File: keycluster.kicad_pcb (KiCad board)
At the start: 2 copper layers, 45.1 x 52.6 mm, 62 parts, among them P2 CONN_5, P7 CONN_10, P8 CONN_7, U1 MKL03Z32VFK4, U2 IS31FL3737, U4 ESD

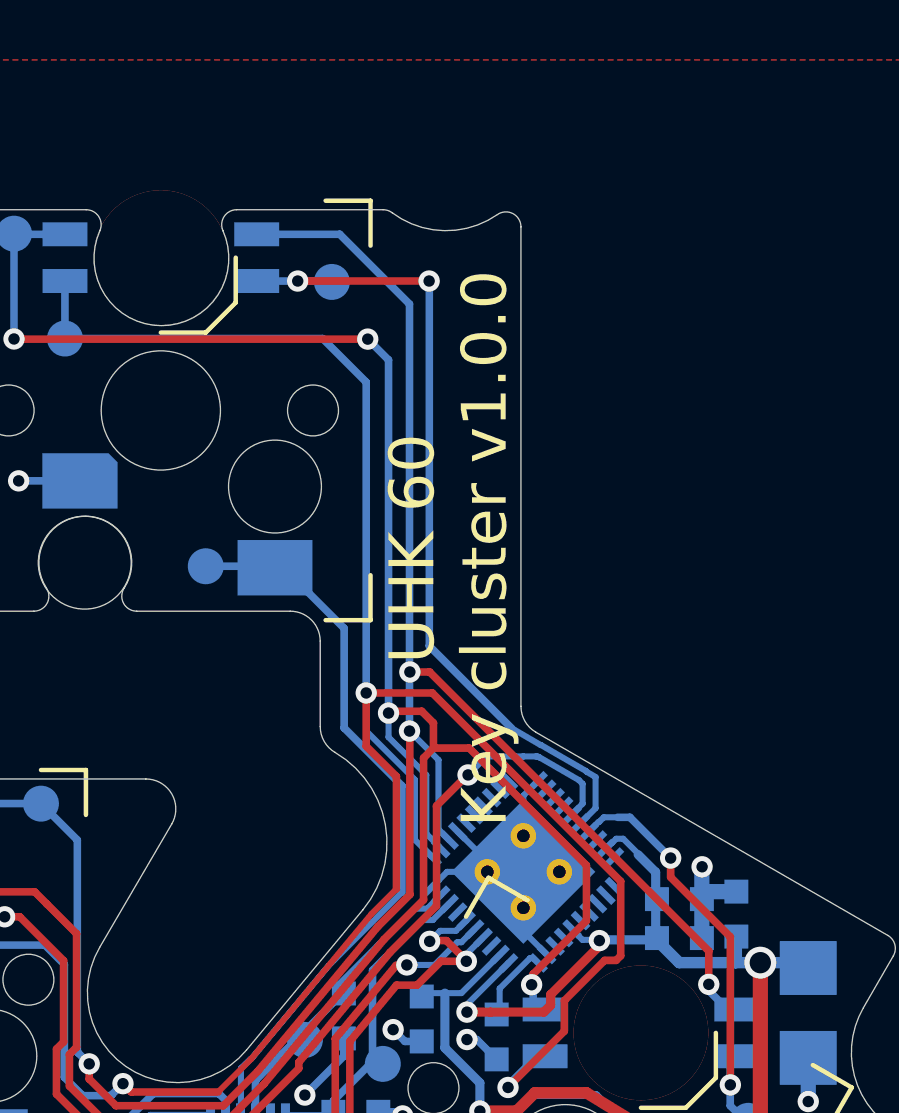
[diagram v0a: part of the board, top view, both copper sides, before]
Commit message: Improve silk screen.
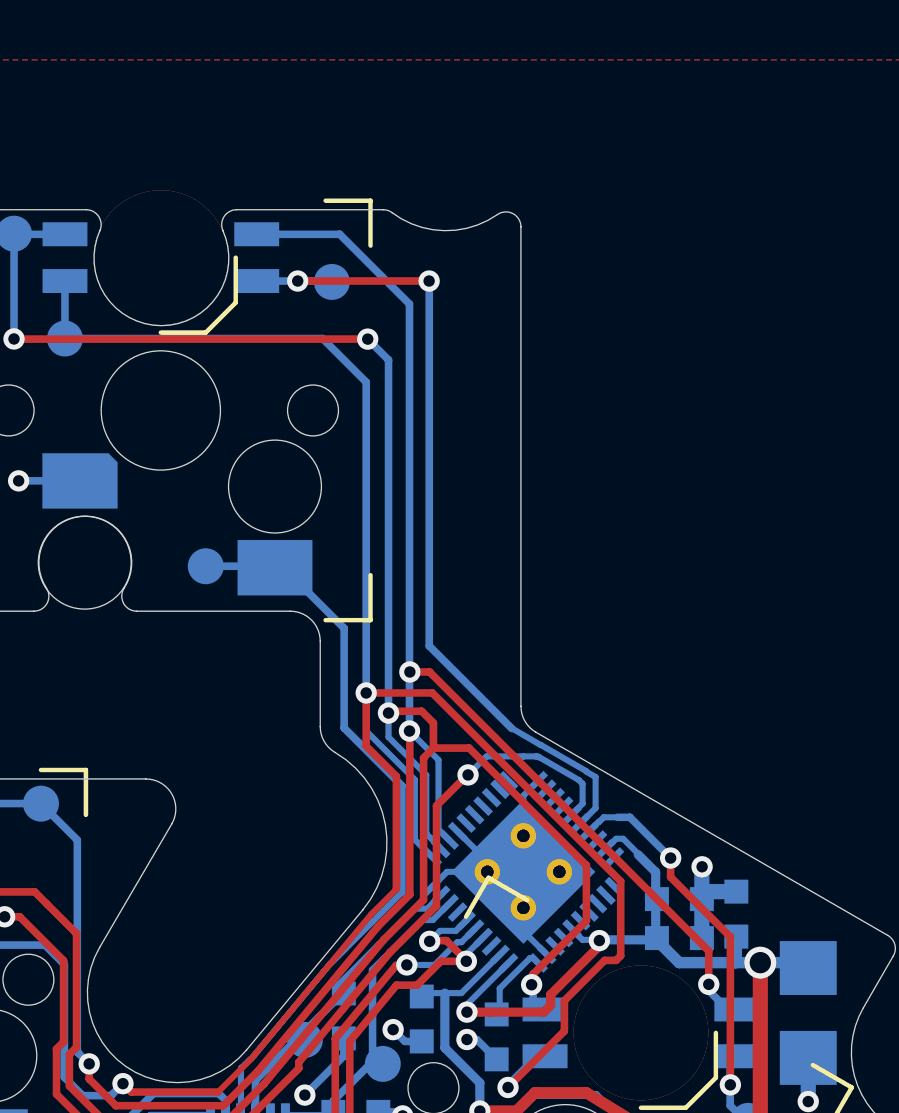
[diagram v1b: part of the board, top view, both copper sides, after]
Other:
- board text added: "PCB ID: keycluster_main_1.0.0"
- board text removed: "UHK 60 Key cluster v1.0.0"
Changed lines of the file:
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@@
     (pcb_text_size 1.5 1.5)
     (mod_edge_width 0.15)
-    (mod_text_size 1 1)
+    (mod_text_size 0.75 0.75)
     (mod_text_width 0.15)
     (pad_size 1.5 1.5)
@@
       (effects (font (size 0.75 0.75) (thickness 0.15)) (justify mirror))
     )
-    (fp_text value GND (at 0 1.3) (layer B.SilkS)
+    (fp_text value GND (at -1.4 1.3) (layer B.SilkS)
       (effects (font (size 0.75 0.75) (thickness 0.15)) (justify mirror))
     )
@@
     )
   )
-  (gr_text "UHK 60\nKey cluster v1.0.0" (at 152.309512 92.310302 90) (layer F.SilkS)
-    (effects (font (size 1.5 1.5) (thickness 0.3)))
+  (gr_text "PCB ID: keycluster_main_1.0.0" (at 164.809512 121.810302 240) (layer B.SilkS)
+    (effects (font (size 0.75 0.75) (thickness 0.15)) (justify mirror))
   )
   (gr_line (start 129.009512 114.110302) (end 132.809512 113.310302) (layer B.SilkS) (width 0.2))

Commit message: Show silk screen values.
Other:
- board text added: "U1 P/N:"

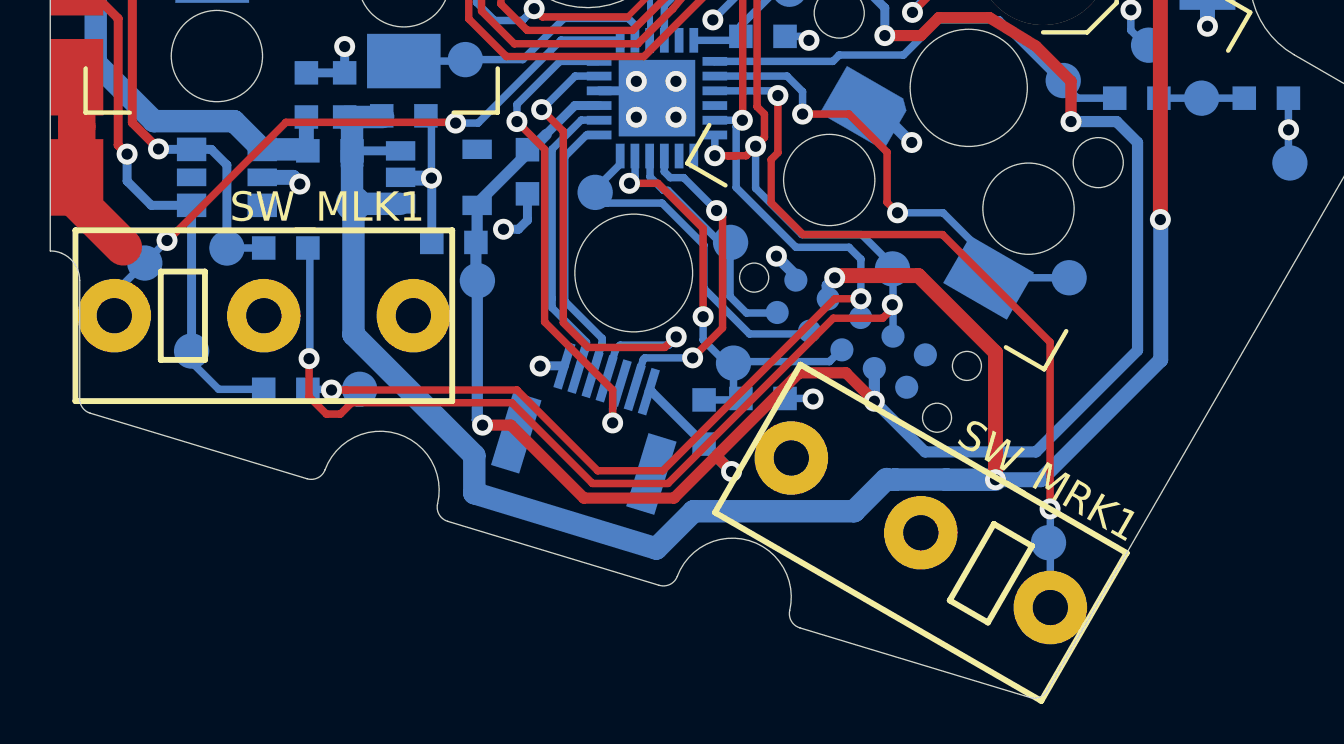
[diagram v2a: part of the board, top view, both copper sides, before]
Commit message: Update buttons.
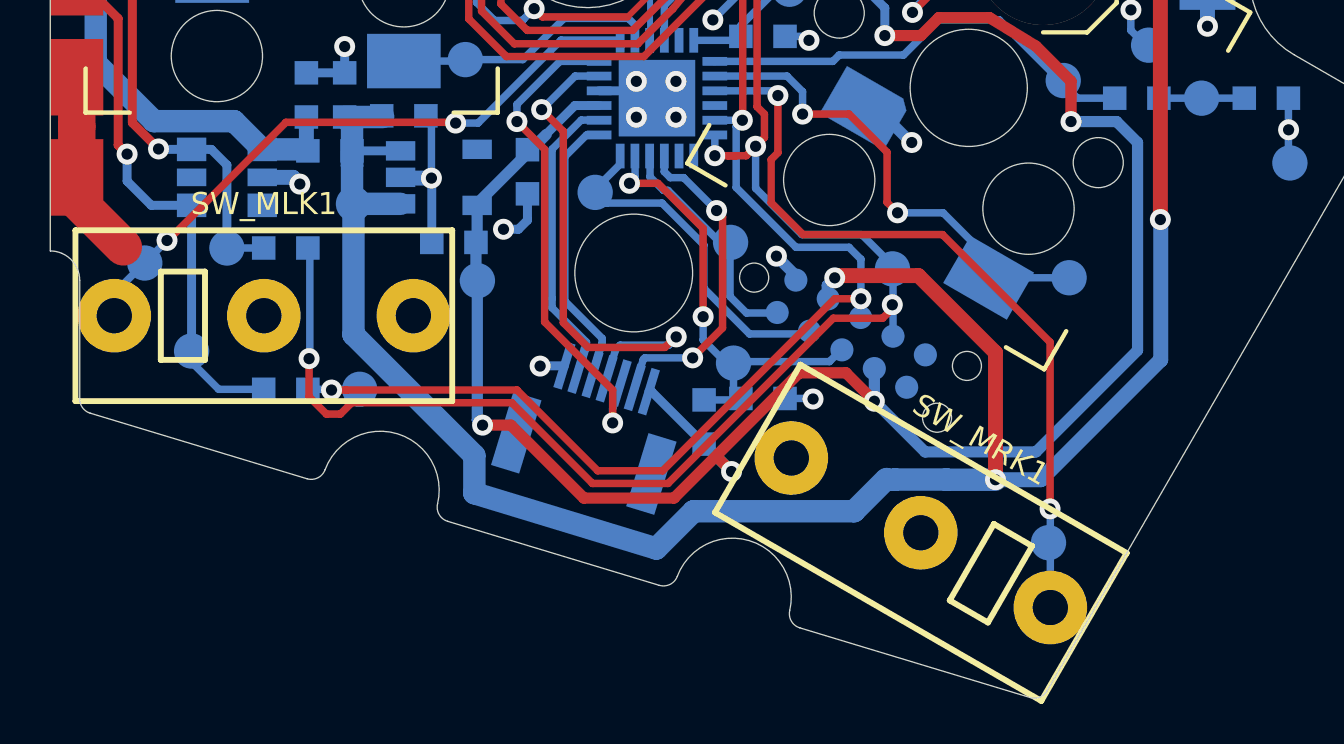
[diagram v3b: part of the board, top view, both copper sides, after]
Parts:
- SW_MLK1, SW_MRK1: footprint ugl:CMI126603D08 -> UGL:CMI126603D08
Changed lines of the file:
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@@
     (add_net "Net-(VR1-Pad4)")
+  )
+  (module UGL:CMI126603D08 locked (layer F.Cu)
+    (at 154.572235 127.973381 150)
+    (fp_text reference SW_MRK1 (at -0.182794 3.757945 150) (layer F.SilkS)
+      (effects (font (size 0.75 0.75) (thickness 0.15)))
+    )
+    (fp_text value MRK (at 0 3.9 150) (layer F.Fab) hide
+      (effects (font (size 0.75 0.75) (thickness 0.15)))
+    )
+    (fp_line (start -3.5 1.5) (end -3.5 -1.5) (layer F.SilkS) (width 0.2))
+    (fp_line (start -2 1.5) (end -3.5 1.5) (layer F.SilkS) (width 0.2))
+    (fp_line (start -2 -1.5) (end -2 1.5) (layer F.SilkS) (width 0.2))
+    (fp_line (start -3.5 -1.5) (end -2 -1.5) (layer F.SilkS) (width 0.2))
+    (fp_line (start 6.4 -2.9) (end 6.4 2.9) (layer F.SilkS) (width 0.2))
+    (fp_line (start -6.4 2.9) (end 6.4 2.9) (layer F.SilkS) (width 0.2))
+    (fp_line (start -6.4 -2.9) (end -6.4 2.9) (layer F.SilkS) (width 0.2))
+    (fp_line (start 6.4 -2.9) (end -6.4 -2.9) (layer F.SilkS) (width 0.2))
+    (pad 3 thru_hole circle (at 5.08 0 150) (size 2.5 2.5) (drill 1.2) (layers *.Cu *.Mask))
+    (pad 2 thru_hole circle (at 0 0 150) (size 2.5 2.5) (drill 1.2) (layers *.Cu *.Mask)
+      (net 1 GND))
+    (pad 1 thru_hole circle (at -5.08 0 150) (size 2.5 2.5) (drill 1.2) (layers *.Cu *.Mask)
+      (net 6 /KEY_MRIGHT))
+  )
+  (module UGL:CMI126603D08 locked (layer F.Cu)
+    (at 132.254409 120.600007)
+    (fp_text reference SW_MLK1 (at 0 -3.8) (layer F.SilkS)
+      (effects (font (size 0.75 0.75) (thickness 0.15)))
+    )
+    (fp_text value MLK (at 0 3.9) (layer F.Fab) hide
+      (effects (font (size 0.75 0.75) (thickness 0.15)))
+    )
+    (fp_line (start -3.5 1.5) (end -3.5 -1.5) (layer F.SilkS) (width 0.2))
+    (fp_line (start -2 1.5) (end -3.5 1.5) (layer F.SilkS) (width 0.2))
+    (fp_line (start -2 -1.5) (end -2 1.5) (layer F.SilkS) (width 0.2))
+    (fp_line (start -3.5 -1.5) (end -2 -1.5) (layer F.SilkS) (width 0.2))
+    (fp_line (start 6.4 -2.9) (end 6.4 2.9) (layer F.SilkS) (width 0.2))
+    (fp_line (start -6.4 2.9) (end 6.4 2.9) (layer F.SilkS) (width 0.2))
+    (fp_line (start -6.4 -2.9) (end -6.4 2.9) (layer F.SilkS) (width 0.2))
+    (fp_line (start 6.4 -2.9) (end -6.4 -2.9) (layer F.SilkS) (width 0.2))
+    (pad 3 thru_hole circle (at 5.08 0) (size 2.5 2.5) (drill 1.2) (layers *.Cu *.Mask))
+    (pad 2 thru_hole circle (at 0 0) (size 2.5 2.5) (drill 1.2) (layers *.Cu *.Mask)
+      (net 1 GND))
+    (pad 1 thru_hole circle (at -5.08 0) (size 2.5 2.5) (drill 1.2) (layers *.Cu *.Mask)
+      (net 5 /KEY_MLEFT))
   )
   (module UGL:hole_4.0mm locked (layer F.Cu)
@@
       (net 5 /KEY_MLEFT))
   )
-  (module ugl:CMI126603D08 locked (layer F.Cu)
-    (at 154.572235 127.973381 150)
-    (fp_text reference SW_MRK1 (at -2.874653 3.69551 150) (layer F.SilkS)
-      (effects (font (size 1 1) (thickness 0.15)))
-    )
-    (fp_text value MRK (at 0 8.8 150) (layer F.Fab) hide
-      (effects (font (size 1 1) (thickness 0.15)))
-    )
-    (fp_line (start -3.5 1.5) (end -3.5 -1.5) (layer F.SilkS) (width 0.2))
-    (fp_line (start -2 1.5) (end -3.5 1.5) (layer F.SilkS) (width 0.2))
-    (fp_line (start -2 -1.5) (end -2 1.5) (layer F.SilkS) (width 0.2))
-    (fp_line (start -3.5 -1.5) (end -2 -1.5) (layer F.SilkS) (width 0.2))
-    (fp_line (start 6.4 -2.9) (end 6.400001 2.9) (layer F.SilkS) (width 0.2))
-    (fp_line (start -6.4 2.9) (end 6.400001 2.9) (layer F.SilkS) (width 0.2))
-    (fp_line (start -6.400001 -2.9) (end -6.4 2.9) (layer F.SilkS) (width 0.2))
-    (fp_line (start 6.4 -2.9) (end -6.400001 -2.9) (layer F.SilkS) (width 0.2))
-    (pad 3 thru_hole circle (at 5.08 0 150) (size 2.5 2.5) (drill 1.2) (layers *.Cu *.Mask))
-    (pad 2 thru_hole circle (at 0 0 150) (size 2.5 2.5) (drill 1.2) (layers *.Cu *.Mask)
-      (net 1 GND))
-    (pad 1 thru_hole circle (at -5.08 0 150) (size 2.5 2.5) (drill 1.2) (layers *.Cu *.Mask)
-      (net 6 /KEY_MRIGHT))
-  )
   (module UGL:Test_Point (layer B.Cu)
     (at 147.509512 108.710302)
@@
       (net 4 /VCC_BOTTOM))
   )
-  (module ugl:CMI126603D08 locked (layer F.Cu)
-    (at 132.254409 120.600007)
-    (fp_text reference SW_MLK1 (at 2.155103 -3.689705 180) (layer F.SilkS)
-      (effects (font (size 1 1) (thickness 0.15)))
-    )
-    (fp_text value MLK (at 0 8.8) (layer F.Fab) hide
-      (effects (font (size 1 1) (thickness 0.15)))
-    )
-    (fp_line (start 6.4 -2.9) (end -6.4 -2.9) (layer F.SilkS) (width 0.2))
-    (fp_line (start -6.4 -2.9) (end -6.4 2.9) (layer F.SilkS) (width 0.2))
-    (fp_line (start -6.4 2.9) (end 6.4 2.9) (layer F.SilkS) (width 0.2))
-    (fp_line (start 6.4 -2.9) (end 6.4 2.9) (layer F.SilkS) (width 0.2))
-    (fp_line (start -3.5 -1.5) (end -2 -1.5) (layer F.SilkS) (width 0.2))
-    (fp_line (start -2 -1.5) (end -2 1.5) (layer F.SilkS) (width 0.2))
-    (fp_line (start -2 1.5) (end -3.5 1.5) (layer F.SilkS) (width 0.2))
-    (fp_line (start -3.5 1.5) (end -3.5 -1.5) (layer F.SilkS) (width 0.2))
-    (pad 1 thru_hole circle (at -5.08 0) (size 2.5 2.5) (drill 1.2) (layers *.Cu *.Mask)
-      (net 5 /KEY_MLEFT))
-    (pad 2 thru_hole circle (at 0 0) (size 2.5 2.5) (drill 1.2) (layers *.Cu *.Mask)
-      (net 1 GND))
-    (pad 3 thru_hole circle (at 5.08 0) (size 2.5 2.5) (drill 1.2) (layers *.Cu *.Mask))
-  )
   (module UGL:FFC_Connector_51281-0794 locked (layer B.Cu)
